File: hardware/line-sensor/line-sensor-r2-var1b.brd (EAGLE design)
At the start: 112 x 60 mm, 120 parts, among them IC1 GP2S60, IC10 GP2S60, IC11 GP2S60, IC12 GP2S60, IC13 GP2S60, IC14 GP2S60, IC15 GP2S60, IC16 GP2S60, IC17 GP2S60, IC18 GP2S60, IC19 GP2S60, IC2 GP2S60, IC20 GP2S60, IC21 GP2S60, IC22 GP2S60, IC23 GP2S60, IC24 GP2S60, IC25 GP2S60, IC26 STM32L151VE, IC27 TI-LM5165YDRCR, IC28 TI-TPS62170, IC29 AD-REF196GSZ, IC3 GP2S60, IC30 AD-ADP124ARHZ, IC4 GP2S60, IC5 GP2S60, IC6 GP2S60, IC7 GP2S60, IC8 GP2S60, IC9 GP2S60, J1 MOLEX-502382-02XX, J2 MOLEX-502382-05XX, J3 MOLEX-53261-0771

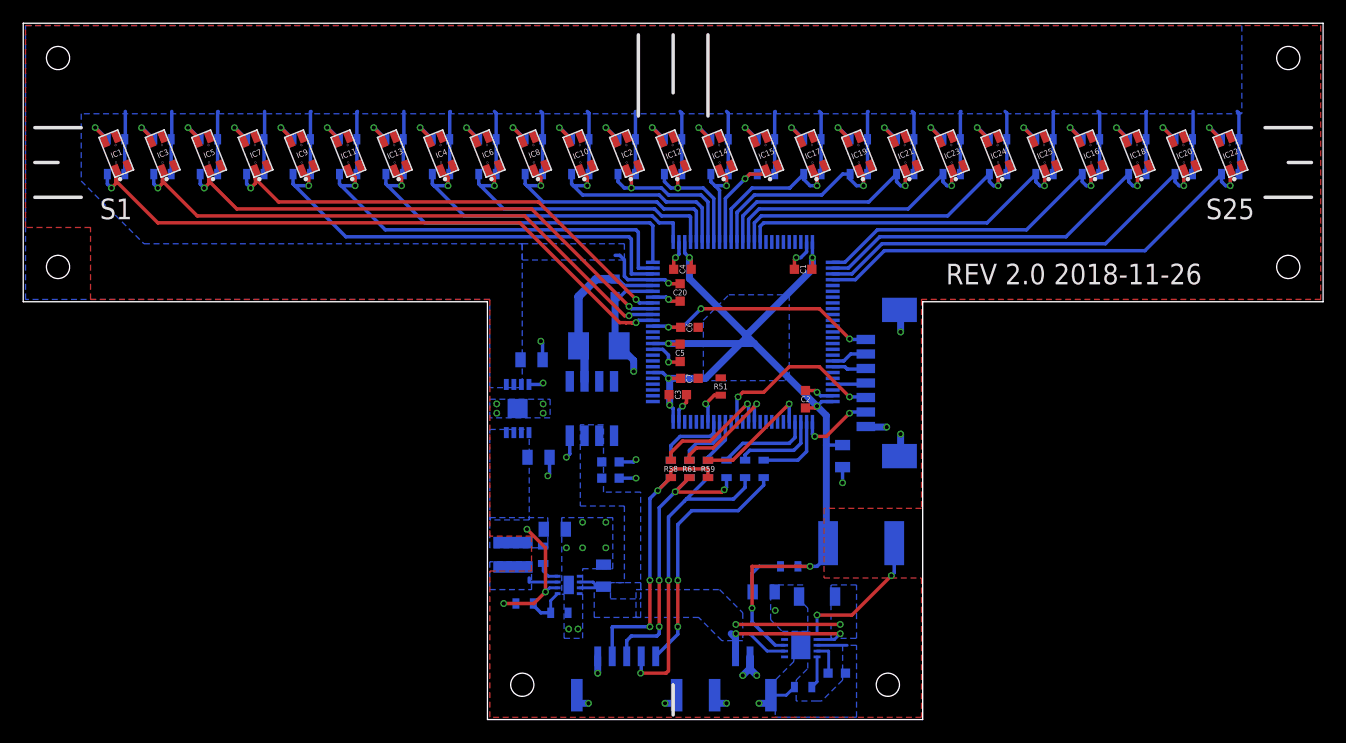
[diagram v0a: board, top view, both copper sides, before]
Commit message: - starting to use TLA for proof of algorithms - fixed line sensor R2 VAR1B schematic a bit (needs a lot more work, after I pick resistor values and voltage ranges) - minor fixes in documentation - migrated deterministic os to latest STM32 package - fixed deterministic os example
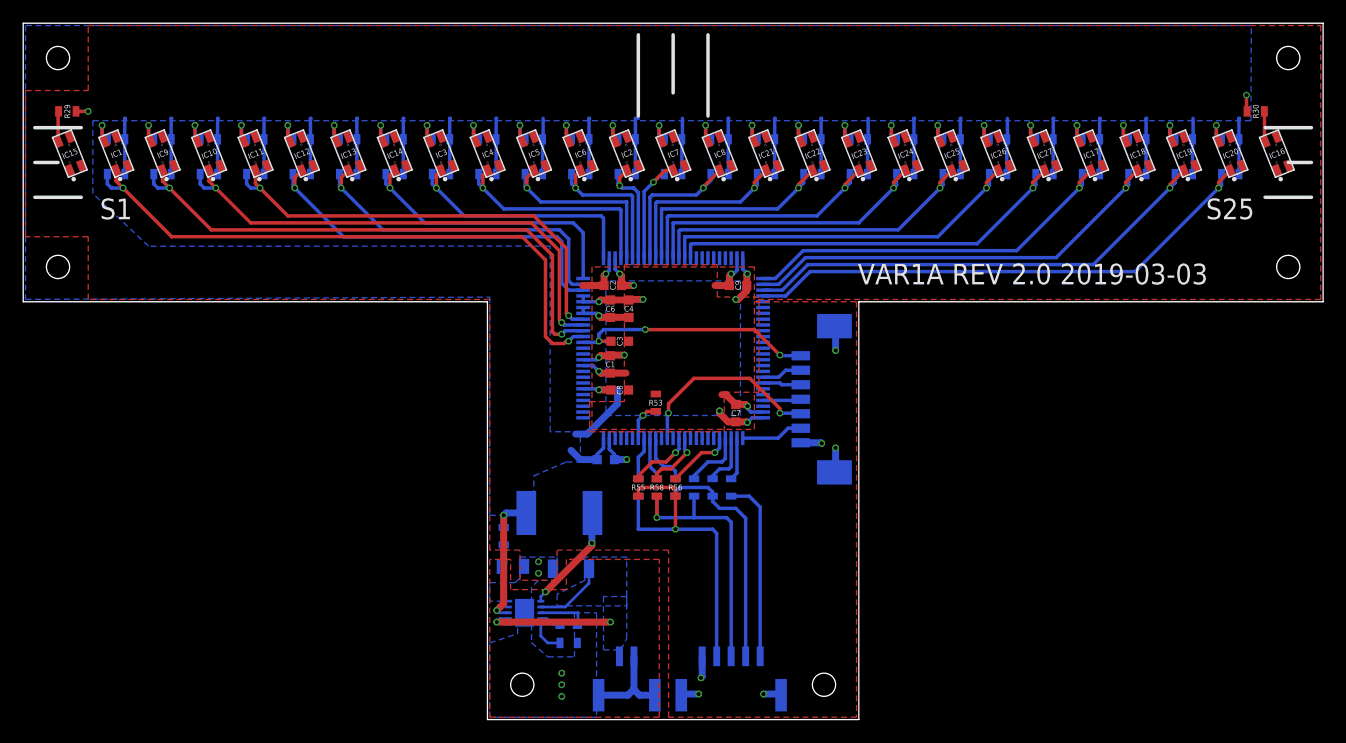
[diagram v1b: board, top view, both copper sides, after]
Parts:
- removed C13: 22u 10V X7R, capacitors:CAPACITOR-0805
- removed C14: 10u 50V, capacitors:CAPACITOR-0603
- removed C15, C18: 1u 10V X7R, capacitors:CAPACITOR-0805
- removed C16: 0.1u 50V, capacitors:CAPACITOR-0603
- removed C17: 1u 10V Tant, capacitors:CAPACITOR_POLARIZED-1411-(3528-MET)
- removed C19, C20: 0.1u 10V X7R, capacitors:CAPACITOR-0603
- removed IC30: AD-ADP124ARHZ, voltage-source:MSOP-8-EP
- removed L2: 150u 0.35A, inductors:ELL-6SH151M
- removed R65: 0, resistors:RESISTOR-0603
- C1, C2, C3, C5, C6, C7: value 0.1u -> 0.1u 10V X7R
- C10: value 33n 10V X7R -> 22u 10V X7S; device capacitors:CAPACITOR-0603 -> passives:CAPACITOR-0805
- C11: value 22u 10V X7S -> 33n 10V X7R; device capacitors:CAPACITOR-0805 -> passives:CAPACITOR-0603
- C12: value 4.7u -> 1u 50V X7R; device capacitors:CAPACITOR-0805 -> passives:CAPACITOR-1206
- C4: value 0.1u -> 1u 10V X7R
- C8: value 10u 50V X7R -> 0.1u 10V X7R; device capacitors:CAPACITOR-0805 -> capacitors:CAPACITOR-0603
- C9: value 1u 50V X7R -> 0.1u 10V X7R; device capacitors:CAPACITOR-1206 -> capacitors:CAPACITOR-0603
- IC26: value STM32L151VE -> GP2S60; device mcu:LQFP100_14X14 -> sensors:GP2S60
- IC27: value TI-LM5165YDRCR -> GP2S60; device voltage-source:VSON-10-0.5MM -> sensors:GP2S60
- IC28: value TI-TPS62170 -> STM32L151VE; device voltage-source:WSON-8-0.5MM -> mcu:LQFP100_14X14
- IC29: value AD-REF196GSZ -> LM5165YDRCR; device voltage-source:SOIC-8 -> voltage-regulator:VSON-10-0.5MM
- J1: value MOLEX-502382-02XX -> MOLEX-502382-05XX; device connectors:MOLEX-502382-02XX -> connectors:MOLEX-502382-05XX
- J2: value MOLEX-502382-05XX -> MOLEX-53261-0771; device connectors:MOLEX-502382-05XX -> connectors:MOLEX-53261-0771
- J3: value MOLEX-53261-0771 -> MOLEX-502382-02XX; device connectors:MOLEX-53261-0771 -> connectors:MOLEX-502382-02XX
- L1: value 3.3u 2.63A -> 150u 0.86R 0.35A; device inductors:VLS3012HBX -> passives:PANASONIC-SERIES-H
- R1: value 1k -> 1k 1% 0.1W
- R10, R14, R18, R22, R26, R34, R38, R42, R6: value 1k -> 220k
- R11, R15, R19, R23, R27, R3, R31, R35, R39, R43, R7: value 220k -> 1k
- R2: value 1k -> 220k 1% 0.1W
- R51: value 100k -> 1k
- R52: value 121k 1% -> 220k
- R53: value 100k 1% -> 100k
- R54: value 0.5 1% -> 0
- R55: value 610k 1% -> 0
- R56: value 180k 1% -> 0
- R63: value 0 -> 121k 1%; device resistors:RESISTOR-0603 -> passives:RESISTOR-0603
- R64: value 0 -> 0.5 5%; device resistors:RESISTOR-0603 -> passives:RESISTOR-0603
- moved R29 60.2 mm to (27.8, 68.4), flipped to the top, turned to 0 degrees
- moved IC15 60.0 mm to (28.0, 64.0)
- moved R52 48.8 mm to (112.0, 63.0), turned to 180 degrees
- moved IC27 46.6 mm to (112.0, 64.0), flipped to the top, turned to 111.8 degrees
- moved R2 44.1 mm to (32.0, 63.0)
- moved R3 44.1 mm to (76.0, 66.0)
- moved R15 40.1 mm to (84.0, 66.0)
- moved R18 36.1 mm to (36.0, 63.0)
- moved R22 36.1 mm to (44.0, 63.0)
- moved R42 36.1 mm to (92.0, 63.0)
- moved IC22 36.0 mm to (92.0, 64.0)
- moved IC7 36.0 mm to (80.0, 64.0)
- moved R13 36.0 mm to (80.0, 66.0)
- moved R40 36.0 mm to (88.0, 63.0)
- moved J3 35.1 mm to (76.0, 16.0), turned to 180 degrees
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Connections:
- removed net IC27_SW: IC27.1, L2.1
- removed net IC28_SW: IC28.7, L1.1
- removed net N$10 (its old number): IC8.4, R14.P$1
- removed net N$13 (its old number): IC12.4, R22.P$1
- removed net N$33: IC27.5, R52.P$1
- removed net N$34: C10.1, IC27.4
- removed net N$36: C11.1, R54.P$2
- removed net N$38: IC28.8, R53.P$1
- removed net N$39: IC28.5, R55.P$1, R56.P$2
- removed net N$8 (its old number): IC4.4, R6.P$1
- removed net VDDA: C18.1, C20.1, IC26.22, IC30.1, IC30.2, IC30.3, R1.P$2, R10.P$2, R11.P$2, R12.P$2, R13.P$2, R14.P$2, R15.P$2, R16.P$2, R17.P$2, R18.P$2, R19.P$2, R2.P$2, R20.P$2, R21.P$2, R22.P$2, R23.P$2, R24.P$2, R25.P$2, R26.P$2, R27.P$2, R28.P$2, R29.P$2, R3.P$2, R30.P$2, R31.P$2, R32.P$2, R33.P$2, R34.P$2, R35.P$2, R36.P$2, R37.P$2, R38.P$2, R39.P$2, R4.P$2, R40.P$2, R41.P$2, R42.P$2, R43.P$2, R44.P$2, R45.P$2, R46.P$2, R47.P$2, R48.P$2, R49.P$2, R5.P$2, R50.P$2, R6.P$2, R7.P$2, R8.P$2, R9.P$2
- removed net VDDA3.5: C13.1, C15.1, IC28.6, IC30.5, IC30.7, IC30.8, L1.2, R53.P$2, R55.P$2
- removed net VREF3.3: C17.POS, C19.1, IC26.21, IC29.6
- new net IC32_SW: IC29.1, L1.1
- new net N$15: IC21.4, R39.P$1
- new net N$22: IC17.4, R31.P$1
- new net N$3: IC10.4, R19.P$1
- new net N$35: IC29.5, R63.P$1
- new net N$40: C11.1, IC29.4
- new net N$42: C10.1, R64.P$2
- new net N$5: IC12.4, R23.P$1
- new net N$7: IC14.4, R27.P$1
- net !RST: now also C3.1, IC28.14, J2.1; no longer C6.1, IC26.14, J3.1
- net BOOT0: now also IC28.94, R53.P$1; no longer IC26.94, R51.P$1
- net GND: now also C12.P$2, C9.2, IC26.2, IC26.3, IC27.2, IC28.10, IC28.19, IC28.20, IC28.27, IC28.49, IC28.74, IC28.99, IC29.10, IC29.3, IC29.PAD, J1.1, J2.7, J3.2, R53.P$2, R63.P$2; no longer C12.2, C13.2, C14.2, C15.2, C16.2, C17.NEG, C18.2, C19.2, C20.2, C9.P$2, IC26.10, IC26.19, IC26.20, IC26.27, IC26.49, IC26.74, IC26.99, IC27.10, IC27.11, IC28.1, IC28.4, IC28.9, IC29.4, IC30.4, IC30.PAD, J1.2, J2.1, J3.7, R51.P$2, R52.P$2, R56.P$1
- net I2C1_SCL: now also IC28.92, R57.P$1; no longer IC26.92, R60.P$1
- net I2C1_SDA: now also IC28.93, R54.P$1; no longer IC26.93, R57.P$1
- net I2C1_SMBA: now also IC28.91, R61.P$2; no longer IC26.91, R64.P$2
- net N$11: now also IC6.4, R11.P$1; no longer IC10.4, R18.P$1
- net N$12: now also R3.P$1; no longer R2.P$1
- net N$14: now also IC8.4, R15.P$1; no longer IC14.4, R26.P$1
- net N$16: now also IC22.4, R41.P$1; no longer IC17.4, R33.P$1
- net N$17: now also IC23.4, R43.P$1; no longer IC19.4, R37.P$1
- net N$18: now also IC24.4, R45.P$1; no longer IC21.4, R41.P$1
- net N$19: now also IC25.4, R47.P$1; no longer IC23.4, R45.P$1
- net N$20: now also IC26.4, R49.P$1; no longer IC24.4, R47.P$1
- net N$21: now also IC27.4, R51.P$1; no longer IC25.4, R49.P$1
- net N$23: now also R33.P$1; no longer R34.P$1
- net N$24: now also IC19.4, R35.P$1; no longer IC20.4, R38.P$1
- net N$25: now also IC20.4, R37.P$1; no longer IC22.4, R42.P$1
- net N$26: now also J1.2, R54.P$2, R55.P$2, R56.P$2; no longer J2.2, R57.P$2, R58.P$2, R59.P$2
- net N$27: now also J1.3, R57.P$2, R58.P$2, R59.P$2; no longer J2.3, R60.P$2, R61.P$2, R62.P$2
- net N$28: now also J1.4, R61.P$1, R62.P$1; no longer J2.4, R63.P$1, R64.P$1
- net N$29: now also J1.5, R60.P$1; no longer J2.5, R65.P$1
- net N$9: now also IC4.4, R7.P$1; no longer IC6.4, R10.P$1
- net SENSOR_1: now also IC28.15, R2.P$1; no longer IC26.15, R3.P$1
- net SENSOR_10: now also IC28.30, IC5.1, R10.P$1; no longer IC26.30, IC8.1, R16.P$1
- net SENSOR_11: now also IC28.31, IC6.1, R12.P$1; no longer IC10.1, IC26.31, R20.P$1
- net SENSOR_12: now also IC28.32; no longer IC26.32
- net SENSOR_13: now also IC28.33, IC7.1, R14.P$1; no longer IC12.1, IC26.33, R24.P$1
- net SENSOR_14: now also IC28.34, IC8.1, R16.P$1; no longer IC14.1, IC26.34, R28.P$1
- net SENSOR_15: now also IC21.1, IC28.35, R40.P$1; no longer IC15.1, IC26.35, R31.P$1
- net SENSOR_16: now also IC22.1, IC28.36, R42.P$1; no longer IC17.1, IC26.36, R35.P$1
- net SENSOR_17: now also IC23.1, IC28.37, R44.P$1; no longer IC19.1, IC26.37, R39.P$1
- net SENSOR_18: now also IC24.1, IC28.38, R46.P$1; no longer IC21.1, IC26.38, R43.P$1
- net SENSOR_19: now also IC25.1, IC28.39, R48.P$1; no longer IC23.1, IC26.39, R46.P$1
- net SENSOR_2: now also IC28.16, IC9.1, R18.P$1; no longer IC26.16, IC3.1, R7.P$1
- net SENSOR_20: now also IC26.1, IC28.40, R50.P$1; no longer IC24.1, IC26.40, R48.P$1
- net SENSOR_21: now also IC27.1, IC28.41, R52.P$1; no longer IC25.1, IC26.41, R50.P$1
- net SENSOR_22: now also IC17.1, IC28.51; no longer IC16.1, IC26.51
- net SENSOR_23: now also IC28.52, R34.P$1; no longer IC26.52, R36.P$1
- net SENSOR_24: now also IC19.1, IC28.53, R36.P$1; no longer IC20.1, IC26.53, R40.P$1
- net SENSOR_25: now also IC20.1, IC28.54, R38.P$1; no longer IC22.1, IC26.54, R44.P$1
- net SENSOR_3: now also IC10.1, IC28.17, R20.P$1; no longer IC26.17, IC5.1, R11.P$1
- net SENSOR_4: now also IC11.1, IC28.18, R22.P$1; no longer IC26.18, IC7.1, R15.P$1
- net SENSOR_5: now also IC12.1, IC28.23, R24.P$1; no longer IC26.23, IC9.1, R19.P$1
- net SENSOR_6: now also IC13.1, IC28.24, R26.P$1; no longer IC11.1, IC26.24, R23.P$1
- net SENSOR_7: now also IC14.1, IC28.25, R28.P$1; no longer IC13.1, IC26.25, R27.P$1
- net SENSOR_8: now also IC28.26, IC3.1, R6.P$1; no longer IC26.26, IC4.1, R8.P$1
- net SENSOR_9: now also IC28.29, IC4.1, R8.P$1; no longer IC26.29, IC6.1, R12.P$1
- net SPI3_MISO: now also IC28.79, R59.P$1; no longer IC26.79, R62.P$1
- net SPI3_MOSI: now also IC28.80, R56.P$1; no longer IC26.80, R59.P$1
- net SPI3_NSS: now also IC28.77, R60.P$2; no longer IC26.77, R65.P$2
- net SPI3_SCK: now also IC28.78, R62.P$2; no longer IC26.78, R63.P$2
- net STLINK_SWO: now also IC28.89, J2.5; no longer IC26.89, J3.5
- net STLINK_TCK: now also IC28.76, J2.6; no longer IC26.76, J3.6
- net STLINK_TMS: now also IC28.72, J2.4; no longer IC26.72, J3.4
- net STLINK_USART1_RX: now also IC28.69, J2.3; no longer IC26.69, J3.3
- net STLINK_USART1_TX: now also IC28.68, J2.2; no longer IC26.68, J3.2
- net USART2_RX: now also IC28.87, R55.P$1; no longer IC26.87, R58.P$1
- net USART2_TX: now also IC28.86, R58.P$1; no longer IC26.86, R61.P$1
- net VBAT: now also C12.P$1, IC29.7, J3.1; no longer C14.1, C16.1, C8.1, C9.P$1, IC27.2, IC27.7, IC28.2, IC28.3, IC29.3, J1.1
- net VDD: now also C6.1, C8.1, C9.1, IC28.100, IC28.11, IC28.21, IC28.22, IC28.28, IC28.50, IC28.6, IC28.75, IC29.8, L1.2, R1.P$2, R10.P$2, R11.P$2, R12.P$2, R13.P$2, R14.P$2, R15.P$2, R16.P$2, R17.P$2, R18.P$2, R19.P$2, R2.P$2, R20.P$2, R21.P$2, R22.P$2, R23.P$2, R24.P$2, R25.P$2, R26.P$2, R27.P$2, R28.P$2, R29.P$2, R3.P$2, R30.P$2, R31.P$2, R32.P$2, R33.P$2, R34.P$2, R35.P$2, R36.P$2, R37.P$2, R38.P$2, R39.P$2, R4.P$2, R40.P$2, R41.P$2, R42.P$2, R43.P$2, R44.P$2, R45.P$2, R46.P$2, R47.P$2, R48.P$2, R49.P$2, R5.P$2, R50.P$2, R51.P$2, R52.P$2, R6.P$2, R64.P$1, R7.P$2, R8.P$2, R9.P$2; no longer C12.1, C3.1, IC26.100, IC26.11, IC26.28, IC26.50, IC26.6, IC26.75, IC27.8, L2.2, R54.P$1
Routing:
- net VDDA: track 143.4 -> 0.00 mm, vias 1 -> 0
- net VDD: track 90.6 -> 174.5 mm, vias 8 -> 15
- net GND: track 63.1 -> 47.7 mm, vias 36 -> 17
- net VREF3.3: track 14.8 -> 0.00 mm
- net VBAT: track 31.1 -> 17.2 mm, vias 4 -> 2
- net VDDA3.5: track 12.3 -> 0.00 mm, vias 3 -> 0
- net IC27_SW: track 12.3 -> 0.00 mm, vias 2 -> 0
- net IC32_SW: track 0.00 -> 9.44 mm, vias 0 -> 2
- net N$28: track 28.3 -> 20.0 mm, vias 2 -> 0
- net SENSOR_15: track 9.47 -> 17.0 mm
- net SENSOR_18: track 19.8 -> 26.5 mm
- net SENSOR_16: track 13.6 -> 20.2 mm
- net SENSOR_19: track 23.2 -> 29.6 mm
- net SENSOR_20: track 26.5 -> 32.8 mm
- net SENSOR_17: track 17.0 -> 23.3 mm
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- removed copper zone on layer 16, net IC28_SW
- removed copper zone on layer 16, net VDDA
- removed copper zone on layer 16, net VDDA3.5
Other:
- outline, holes or cut-outs redrawn
- board text added: "VAR1A REV 2.0 2019-03-03"
- board text removed: "REV 2.0 2018-11-26"
